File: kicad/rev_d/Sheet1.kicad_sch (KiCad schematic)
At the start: 163 parts, among them J1 JUMPER, J2 JUMPER, J3 JUMPER, J4 JUMPER, J7 JUMPER, Q1 14Mhz, X1 FDD34M, X2 IDE40M, X3 IDC26LPT, X7 DB15VGA, X8 PLB1-4I, X9 PLB1-2

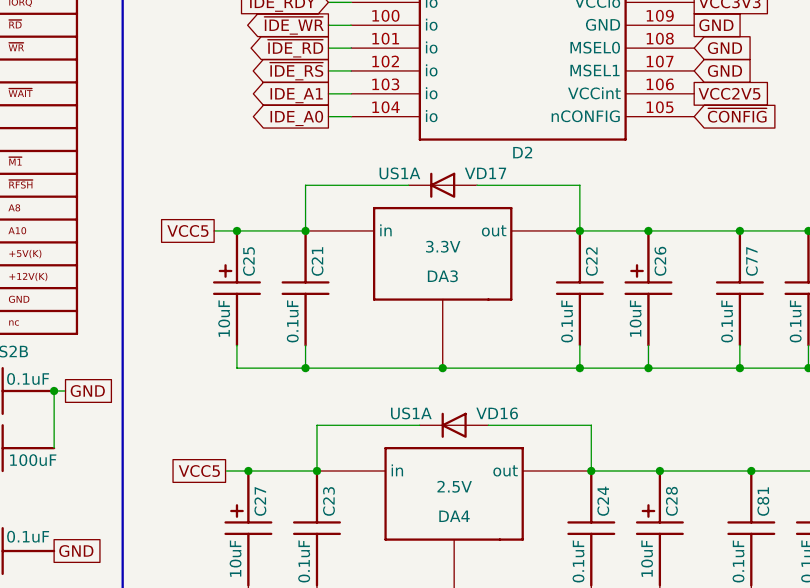
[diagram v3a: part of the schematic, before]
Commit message: pentevo: add datasheets for SS14 and S1A diodes; rev. D: replace linear regulator diodes with S1A
git-svn-id: svn://localhost/local-pentevo@1223 c6c76956-fad2-4150-a3a9-ea0a427205ba
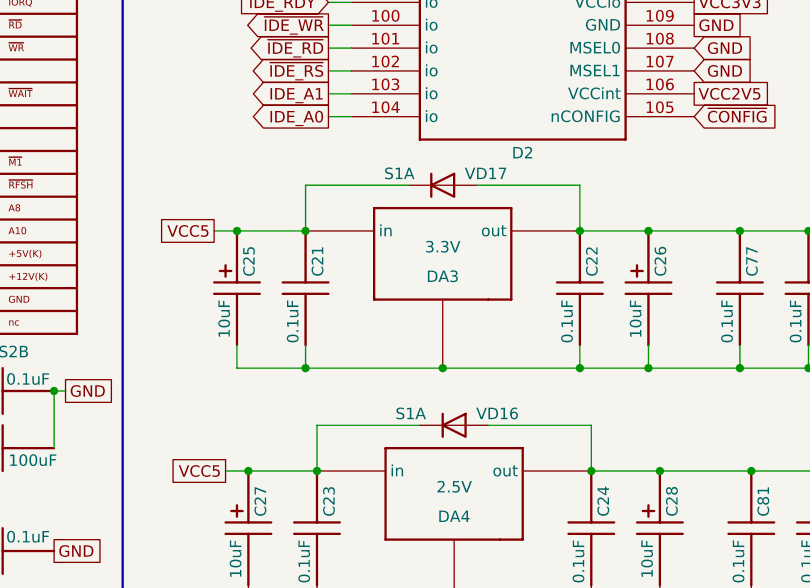
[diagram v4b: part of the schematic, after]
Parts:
- VD16, VD17: value US1A -> S1A
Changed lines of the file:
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@@
 			)
 		)
-		(property "Value" "US1A"
+		(property "Value" "S1A"
 			(at 128.524 386.08 0)
 			(effects
@@
 			)
 		)
-		(property "Value" "US1A"
+		(property "Value" "S1A"
 			(at 127.254 359.41 0)
 			(effects

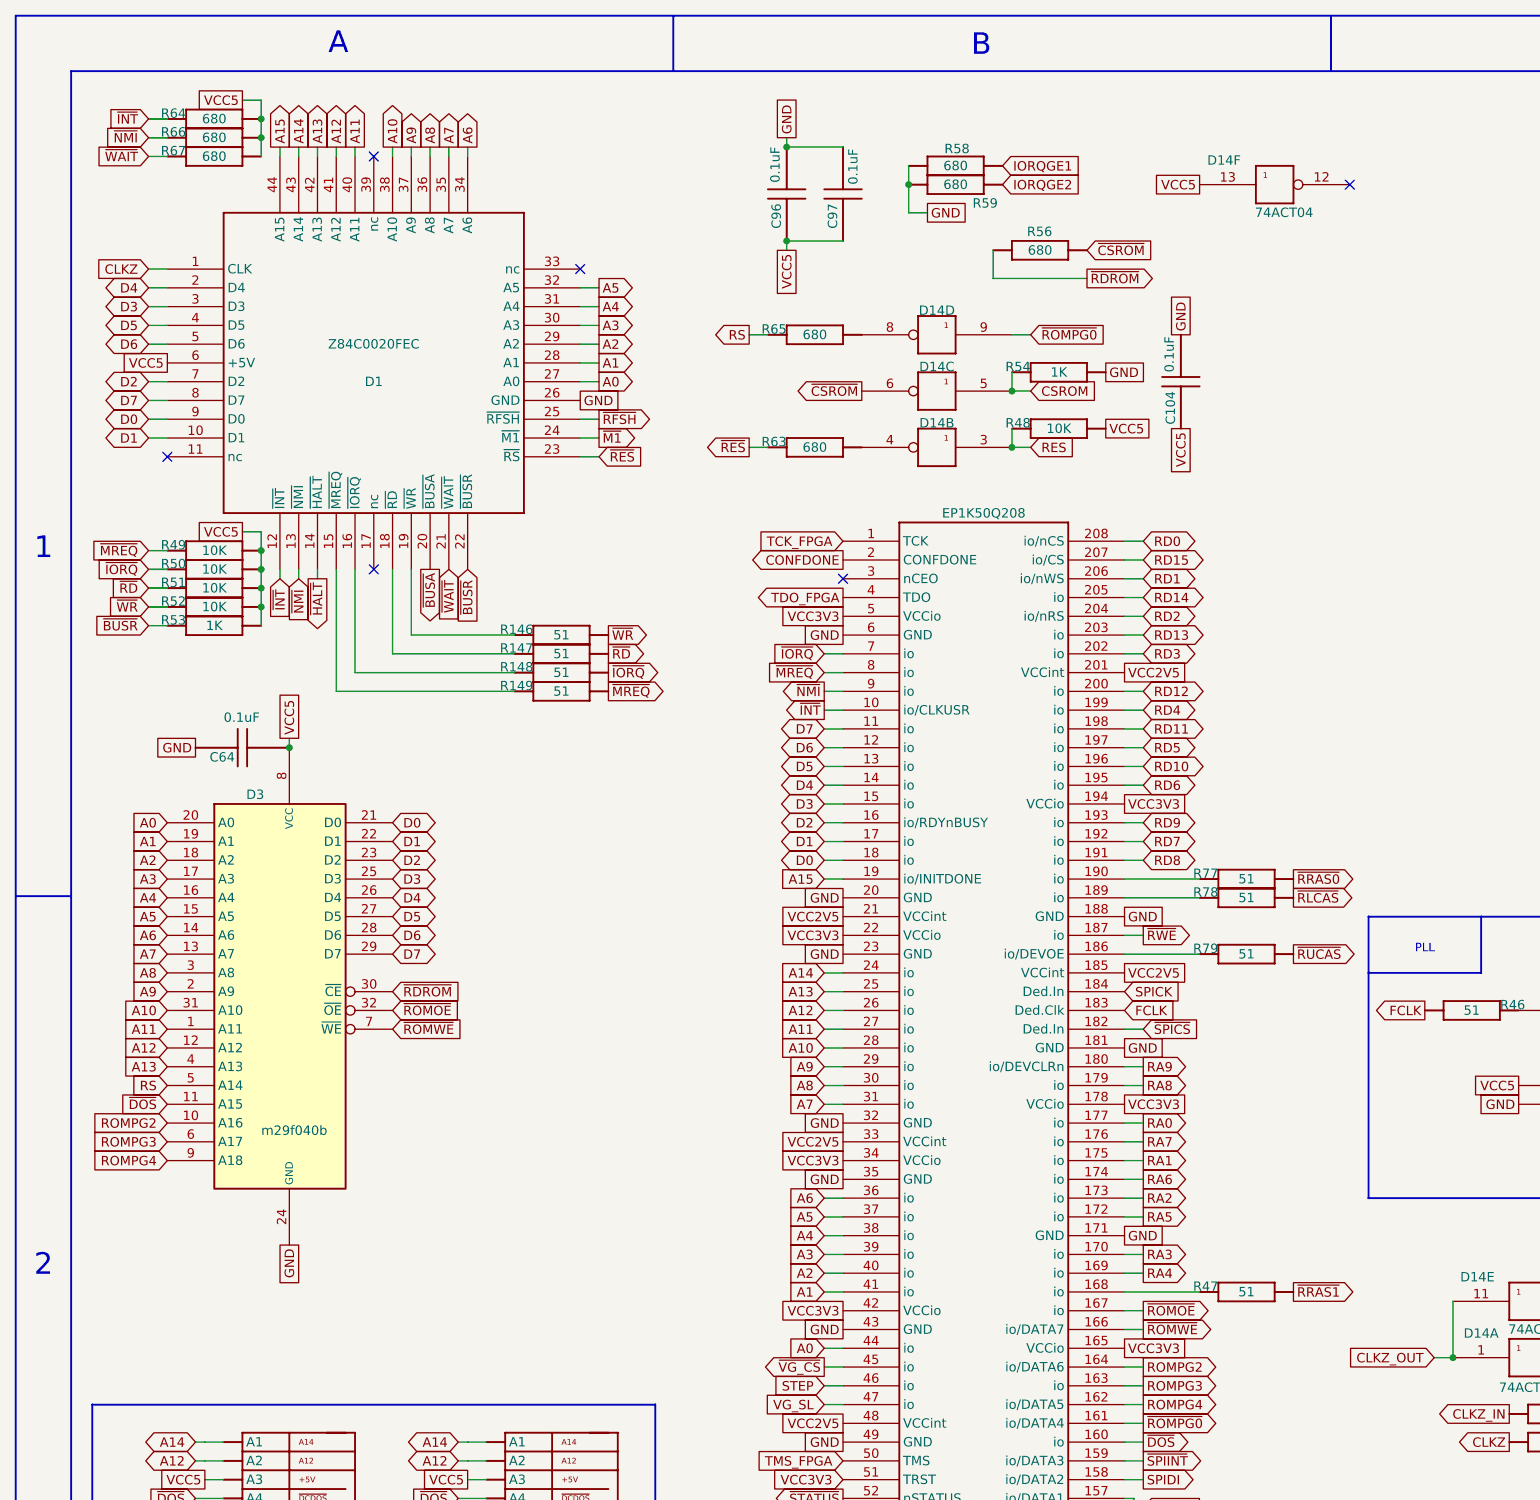
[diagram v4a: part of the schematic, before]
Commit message: pentevo: rev D: replace tlc072 with tlv9162; replace m29f040b to m29f032d; TODO: add pca9555 to control high address pins of flash ic
git-svn-id: svn://localhost/local-pentevo@1227 c6c76956-fad2-4150-a3a9-ea0a427205ba
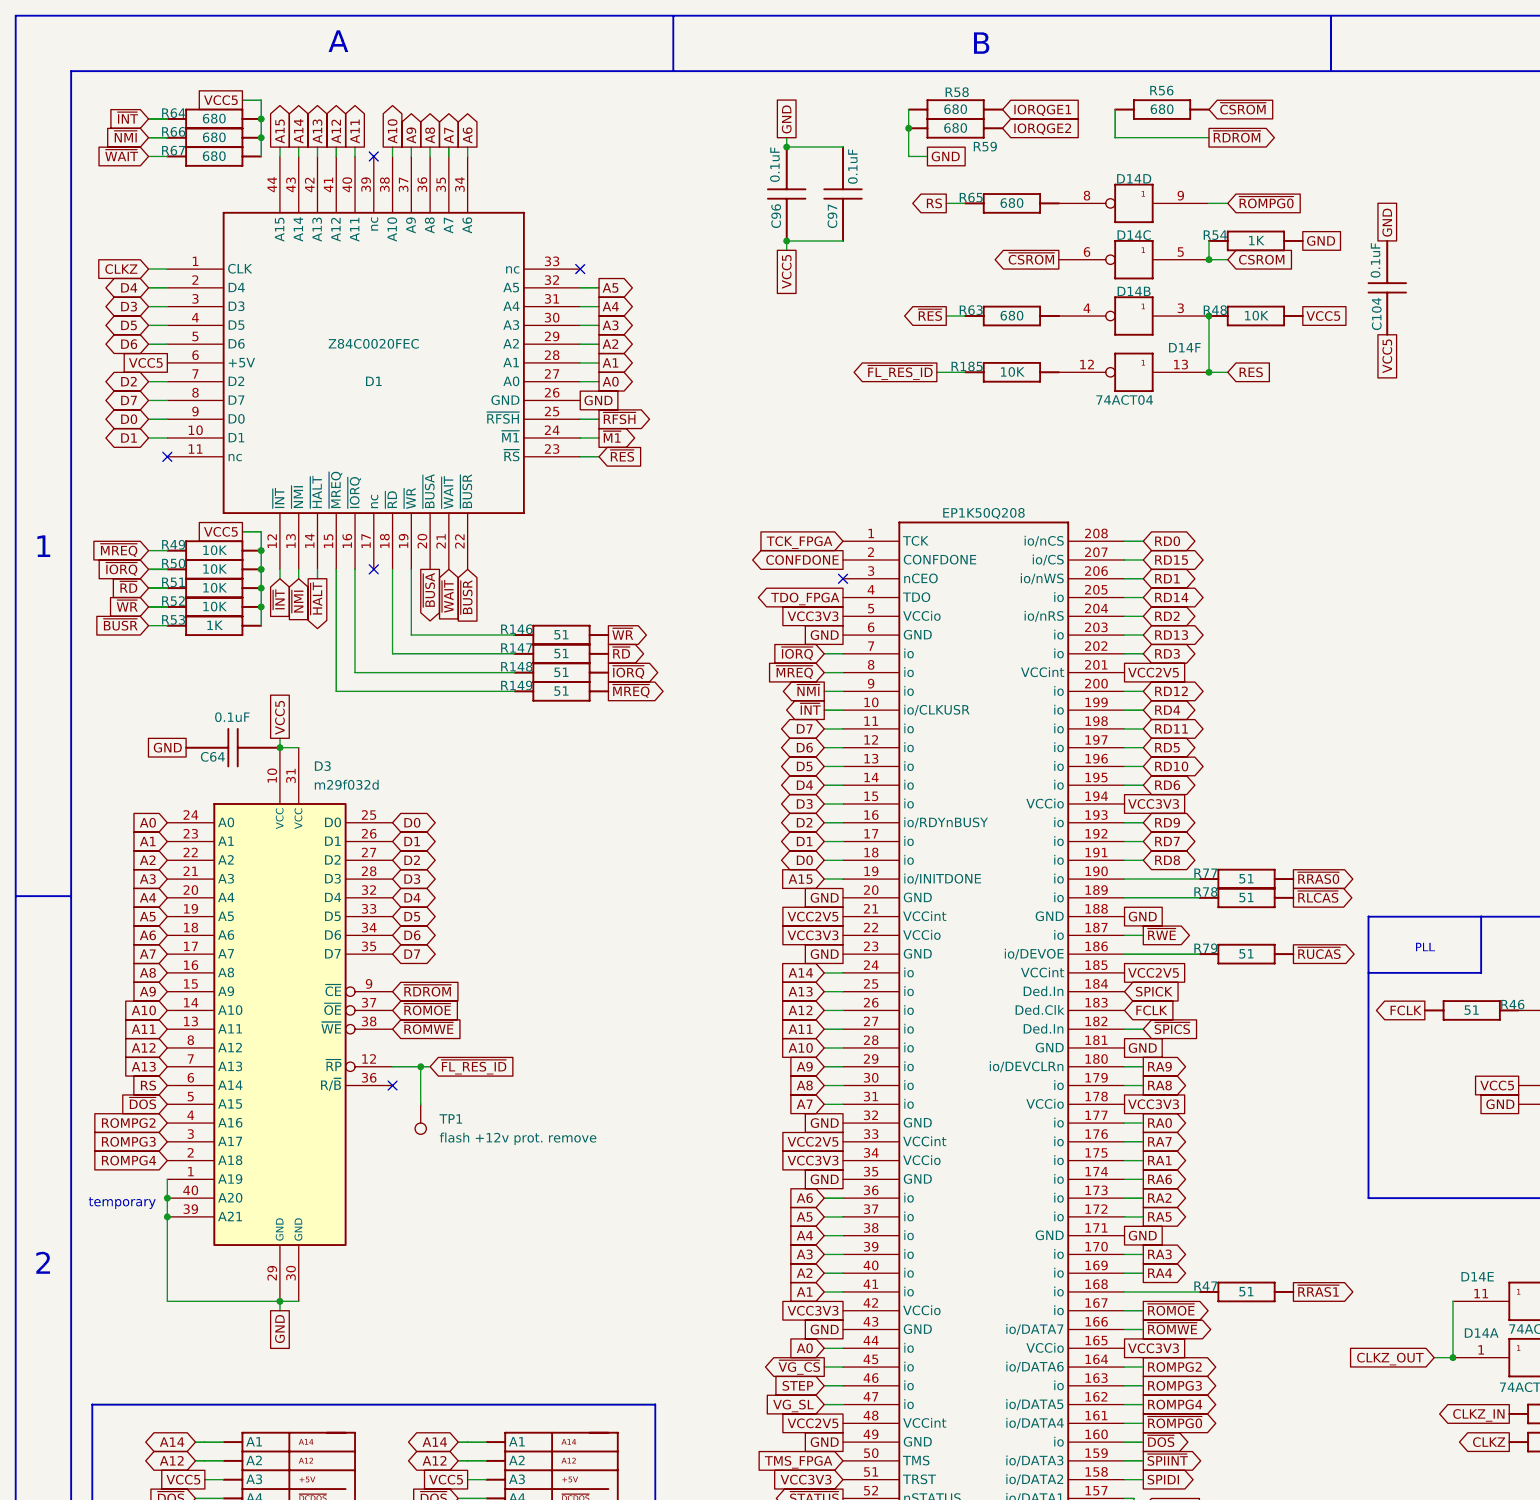
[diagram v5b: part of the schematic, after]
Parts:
- removed D3: m29f040b, Package_SO:TSOP-I-32_18.4x8mm_P0.5mm, symbol Memory_Flash:29W040
- added D3: m29f032d, Package_SO:TSOP-I-40_18.4x10mm_P0.5mm, symbol eva-altium-import:m29f032d
- added R185: 10K, R-CHIP, symbol eva-altium-import:Sheet1_0_RESCHIP
- added TP1: flash +12v prot. remove, TestPoint:TestPoint_THTPad_1.5x1.5mm_Drill0.7mm, symbol Connector:TestPoint
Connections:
- net A0: now also D3.24 (A0)
- net A1: now also D3.23 (A1)
- net A10: now also D3.14 (A10)
- net A11: now also D3.13 (A11)
- net A12: now also D3.8 (A12)
- net A13: now also D3.7 (A13)
- net A2: now also D3.22 (A2)
- net A3: now also D3.21 (A3)
- net A4: now also D3.20 (A4)
- net A5: now also D3.19 (A5)
- net A6: now also D3.18 (A6)
- net A7: now also D3.17 (A7)
- net A8: now also D3.16 (A8)
- net A9: now also D3.15 (A9)
- net D0: now also D3.25 (D0)
- net D1: now also D3.26 (D1)
- net D2: now also D3.27 (D2)
- net D3: now also D3.28 (D3)
- net D4: now also D3.32 (D4)
- net D5: now also D3.33 (D5)
- net D6: now also D3.34 (D6)
- net D7: now also D3.35 (D7)
- net GND: now also D3.1 (A19), D3.29 (GND), D3.30 (GND), D3.39 (A21), D3.40 (A20)
- net RES: now also D14.13
- net ROMPG2: now also D3.4 (A16)
- net ROMPG3: now also D3.3 (A17)
- net ROMPG4: now also D3.2 (A18)
- net RS: now also D3.6 (A14)
- net VCC5: now also D3.10 (VCC), D3.31 (VCC); no longer D14.13
- net ~{DOS}: now also D3.5 (A15)
- net ~{RDROM}: now also D3.9 (~{CE})
- net ~{ROMOE}: now also D3.37 (~{OE})
- net ~{ROMWE}: now also D3.38 (~{WE})
- net at D14.12: now also R185.1 (i/o)
- new net ~{FL_RES_ID}: D3.12 (~{RP}), R185.2 (i/o1), TP1.1
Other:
- note added: "temporary"
- moved on the sheet: C104, C64, D14B, D14C, D14D, D14F, R48, R54, R56, R58, R59, R63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
